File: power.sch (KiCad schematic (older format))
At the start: 25 parts

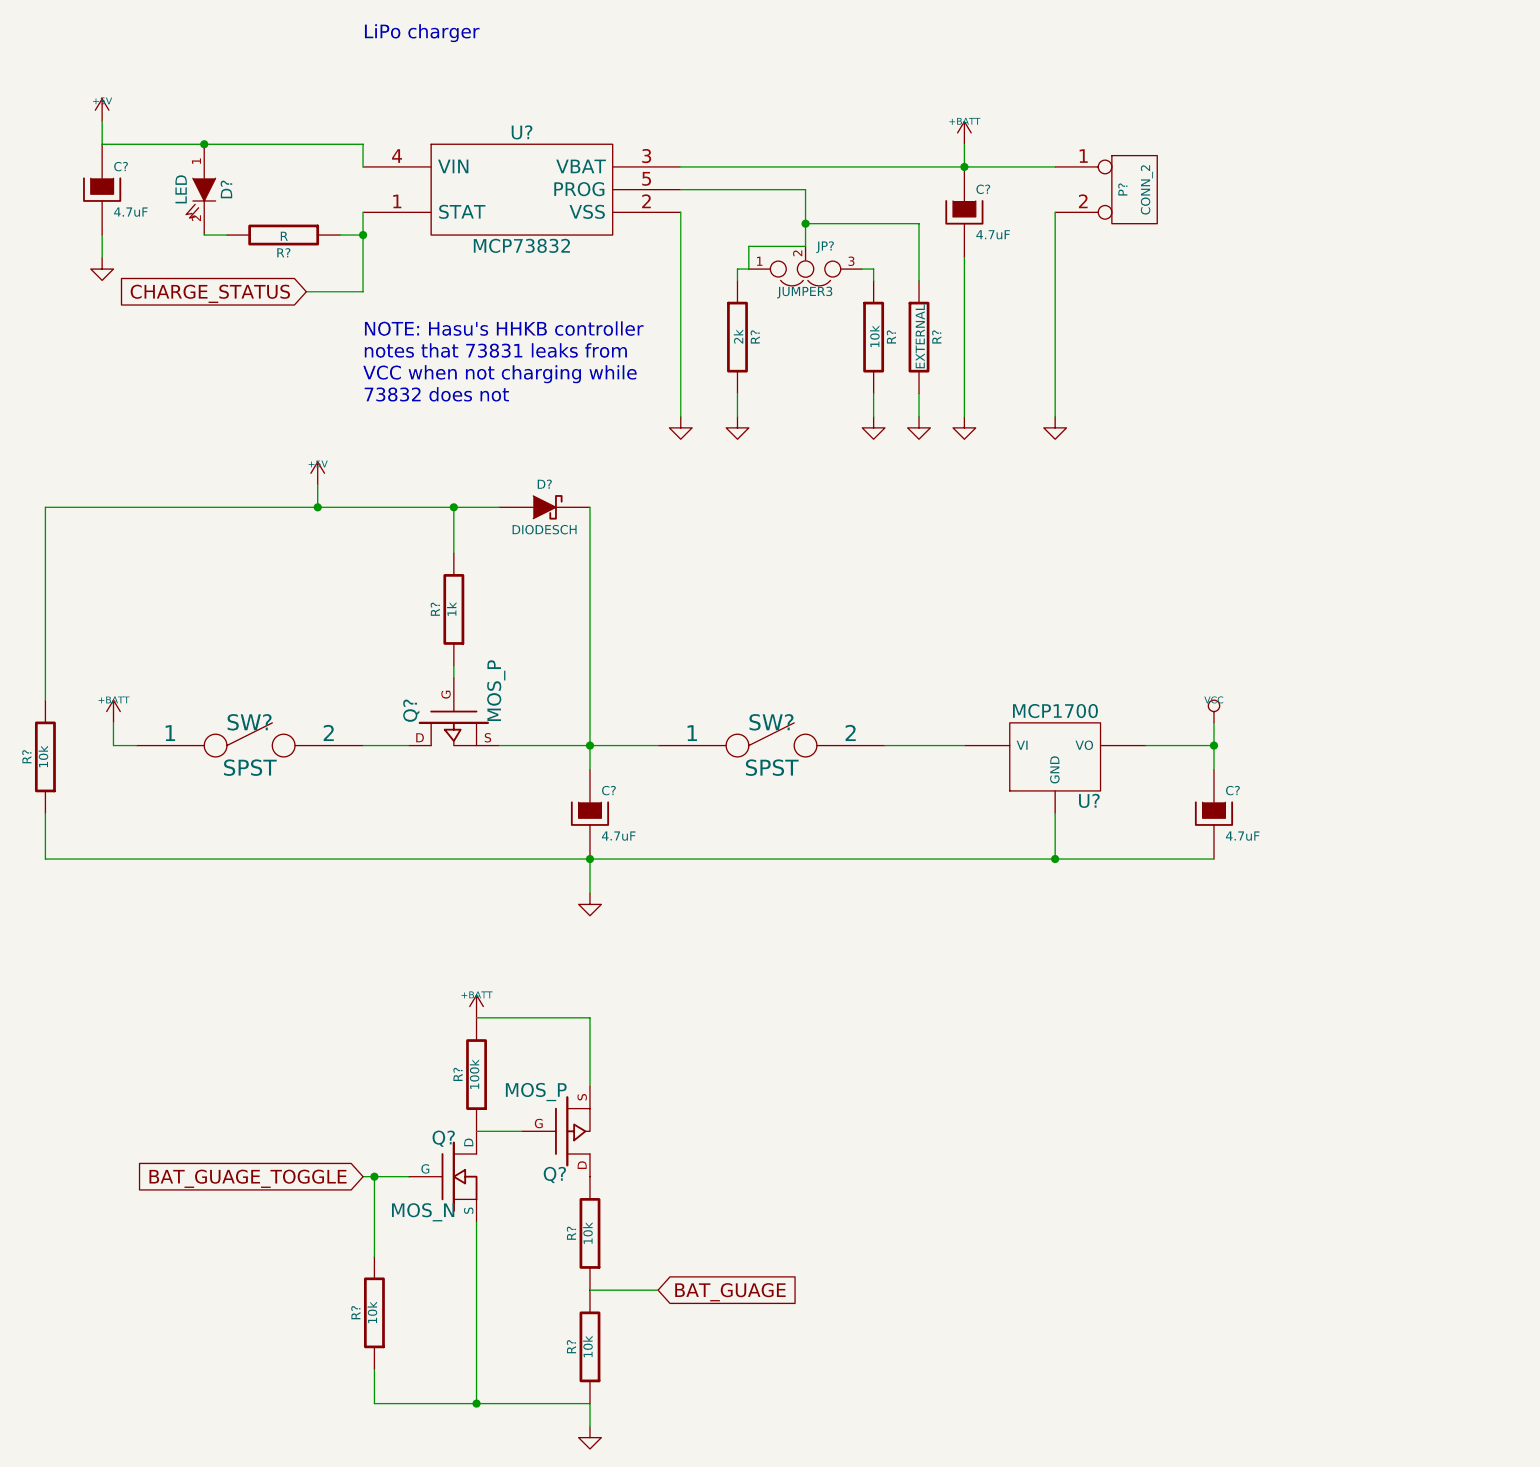
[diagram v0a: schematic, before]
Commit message: Add annotations to parts
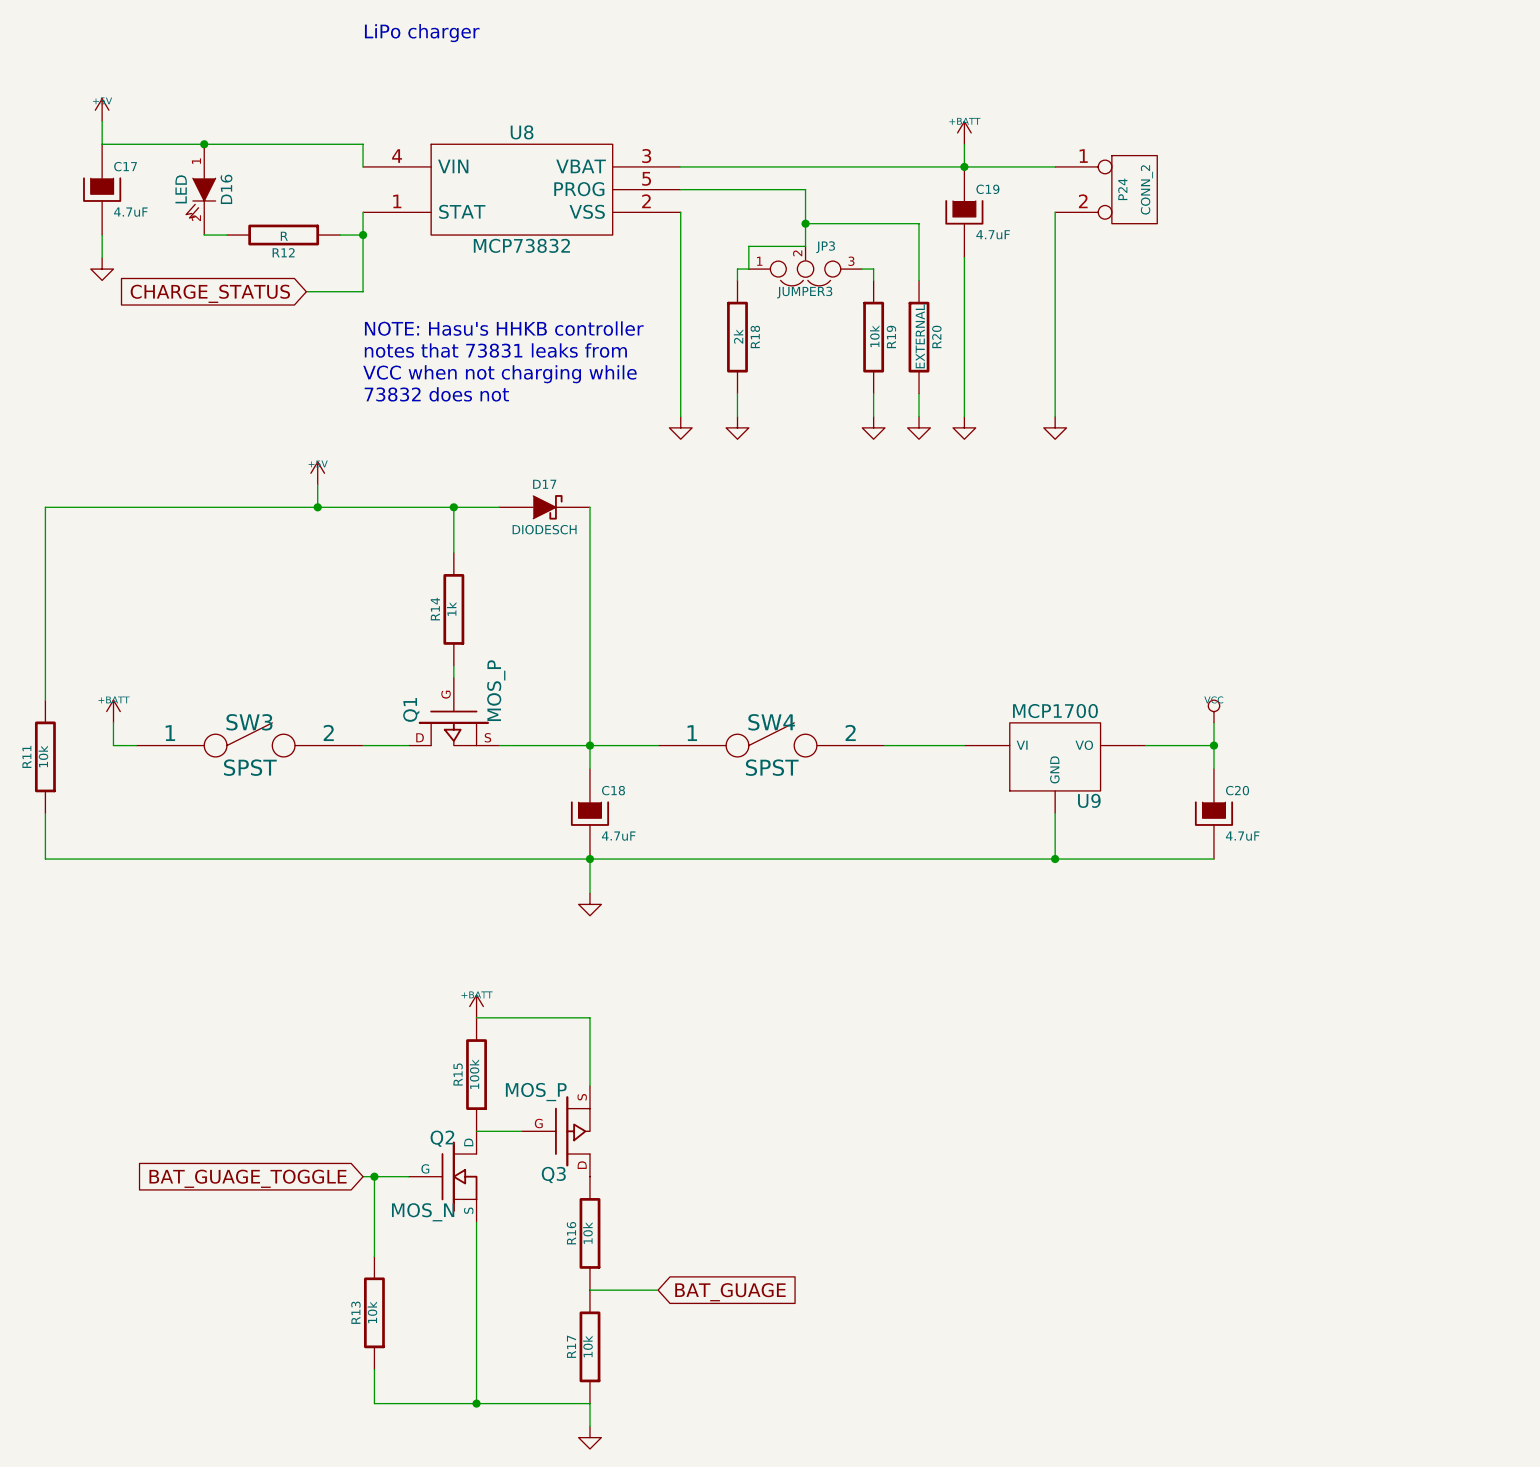
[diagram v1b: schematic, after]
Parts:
- gave numbers to parts that had none: 25
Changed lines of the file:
@@
 $EndDescr
 $Comp
-L +5V #PWR?
+L +5V #PWR56
 U 1 1 54E62CDB
 P 1050 1250
-F 0 "#PWR?" H 1050 1340 20  0001 C CNN
+F 0 "#PWR56" H 1050 1340 20  0001 C CNN
 F 1 "+5V" H 1050 1340 30  0000 C CNN
 F 2 "" H 1050 1250 60  0000 C CNN
@@
 $EndComp
 $Comp
-L GND #PWR?
+L GND #PWR57
 U 1 1 54E62CE1
 P 1050 1850
-F 0 "#PWR?" H 1050 1850 30  0001 C CNN
+F 0 "#PWR57" H 1050 1850 30  0001 C CNN
 F 1 "GND" H 1050 1780 30  0001 C CNN
 F 2 "" H 1050 1850 60  0000 C CNN
@@
 $EndComp
 $Comp
-L CP C?
+L CP C17
 U 1 1 54E62CE7
 P 1050 1550
-F 0 "C?" H 1100 1650 40  0000 L CNN
+F 0 "C17" H 1100 1650 40  0000 L CNN
 F 1 "4.7uF" H 1100 1450 40  0000 L CNN
 F 2 "" H 1150 1400 30  0000 C CNN
@@
 $EndComp
 $Comp
-L LED D?
+L LED D16
 U 1 1 54E62CEE
 P 1500 1550
-F 0 "D?" H 1500 1650 50  0000 C CNN
+F 0 "D16" H 1500 1650 50  0000 C CNN
 F 1 "LED" H 1500 1450 50  0000 C CNN
 F 2 "" H 1500 1550 60  0000 C CNN
@@
 $EndComp
 $Comp
-L MCP73831 U?
+L MCP73831 U8
 U 1 1 54E62CF5
 P 2900 1500
-F 0 "U?" H 2900 1700 60  0000 C CNN
+F 0 "U8" H 2900 1700 60  0000 C CNN
 F 1 "MCP73832" H 2900 1200 60  0000 C CNN
 F 2 "" H 2900 1500 60  0000 C CNN
@@
 $EndComp
 $Comp
-L JUMPER3 JP?
+L JUMPER3 JP3
 U 1 1 54E62CFC
 P 4150 1900
-F 0 "JP?" H 4200 1800 40  0000 L CNN
+F 0 "JP3" H 4200 1800 40  0000 L CNN
 F 1 "JUMPER3" H 4150 2000 40  0000 C CNN
 F 2 "" H 4150 1900 60  0000 C CNN
@@
 $EndComp
 $Comp
-L R R?
+L R R18
 U 1 1 54E62D03
 P 3850 2200
-F 0 "R?" V 3930 2200 40  0000 C CNN
+F 0 "R18" V 3930 2200 40  0000 C CNN
 F 1 "2k" V 3857 2201 40  0000 C CNN
 F 2 "" V 3780 2200 30  0000 C CNN
@@
 $EndComp
 $Comp
-L R R?
+L R R19
 U 1 1 54E62D0A
 P 4450 2200
-F 0 "R?" V 4530 2200 40  0000 C CNN
+F 0 "R19" V 4530 2200 40  0000 C CNN
 F 1 "10k" V 4457 2201 40  0000 C CNN
 F 2 "" V 4380 2200 30  0000 C CNN
@@
 $EndComp
 $Comp
-L R R?
+L R R20
 U 1 1 54E62D11
 P 4650 2200
-F 0 "R?" V 4730 2200 40  0000 C CNN
+F 0 "R20" V 4730 2200 40  0000 C CNN
 F 1 "EXTERNAL" V 4657 2201 40  0000 C CNN
 F 2 "" V 4580 2200 30  0000 C CNN
@@
 $EndComp
 $Comp
-L CP C?
+L CP C19
 U 1 1 54E62D18
 P 4850 1650
-F 0 "C?" H 4900 1750 40  0000 L CNN
+F 0 "C19" H 4900 1750 40  0000 L CNN
 F 1 "4.7uF" H 4900 1550 40  0000 L CNN
 F 2 "" H 4950 1500 30  0000 C CNN
@@
 $EndComp
 $Comp
-L R R?
+L R R12
 U 1 1 54E62D1F
 P 1850 1750
-F 0 "R?" V 1930 1750 40  0000 C CNN
+F 0 "R12" V 1930 1750 40  0000 C CNN
 F 1 "R" V 1857 1751 40  0000 C CNN
 F 2 "" V 1780 1750 30  0000 C CNN
@@
 $EndComp
 $Comp
-L GND #PWR?
+L GND #PWR63
 U 1 1 54E62D26
 P 3600 2550
-F 0 "#PWR?" H 3600 2550 30  0001 C CNN
+F 0 "#PWR63" H 3600 2550 30  0001 C CNN
 F 1 "GND" H 3600 2480 30  0001 C CNN
 F 2 "" H 3600 2550 60  0000 C CNN
@@
 $EndComp
 $Comp
-L GND #PWR?
+L GND #PWR64
 U 1 1 54E62D2C
 P 3850 2550
-F 0 "#PWR?" H 3850 2550 30  0001 C CNN
+F 0 "#PWR64" H 3850 2550 30  0001 C CNN
 F 1 "GND" H 3850 2480 30  0001 C CNN
 F 2 "" H 3850 2550 60  0000 C CNN
@@
 $EndComp
 $Comp
-L GND #PWR?
+L GND #PWR65
 U 1 1 54E62D32
 P 4450 2550
-F 0 "#PWR?" H 4450 2550 30  0001 C CNN
+F 0 "#PWR65" H 4450 2550 30  0001 C CNN
 F 1 "GND" H 4450 2480 30  0001 C CNN
 F 2 "" H 4450 2550 60  0000 C CNN
@@
 $EndComp
 $Comp
-L GND #PWR?
+L GND #PWR66
 U 1 1 54E62D38
 P 4650 2550
-F 0 "#PWR?" H 4650 2550 30  0001 C CNN
+F 0 "#PWR66" H 4650 2550 30  0001 C CNN
 F 1 "GND" H 4650 2480 30  0001 C CNN
 F 2 "" H 4650 2550 60  0000 C CNN
@@
 $EndComp
 $Comp
-L GND #PWR?
+L GND #PWR68
 U 1 1 54E62D3E
 P 4850 2550
-F 0 "#PWR?" H 4850 2550 30  0001 C CNN
+F 0 "#PWR68" H 4850 2550 30  0001 C CNN
 F 1 "GND" H 4850 2480 30  0001 C CNN
 F 2 "" H 4850 2550 60  0000 C CNN
@@
 $EndComp
 $Comp
-L +BATT #PWR?
+L +BATT #PWR67
 U 1 1 54E62D44
 P 4850 1350
-F 0 "#PWR?" H 4850 1300 20  0001 C CNN
+F 0 "#PWR67" H 4850 1300 20  0001 C CNN
 F 1 "+BATT" H 4850 1450 30  0000 C CNN
 F 2 "" H 4850 1350 60  0000 C CNN
@@
 $EndComp
 $Comp
-L CONN_2 P?
+L CONN_2 P24
 U 1 1 54E62D4A
 P 5600 1550
-F 0 "P?" V 5550 1550 40  0000 C CNN
+F 0 "P24" V 5550 1550 40  0000 C CNN
 F 1 "CONN_2" V 5650 1550 40  0000 C CNN
 F 2 "" H 5600 1550 60  0000 C CNN
@@
 $EndComp
 $Comp
-L GND #PWR?
+L GND #PWR69
 U 1 1 54E62D51
 P 5250 2550
-F 0 "#PWR?" H 5250 2550 30  0001 C CNN
+F 0 "#PWR69" H 5250 2550 30  0001 C CNN
 F 1 "GND" H 5250 2480 30  0001 C CNN
 F 2 "" H 5250 2550 60  0000 C CNN
@@
 NOTE: Hasu's HHKB controller\nnotes that 73831 leaks from\nVCC when not charging while\n73832 does not
 $Comp
-L MOS_P Q?
+L MOS_P Q3
 U 1 1 54E64257
 P 3100 5700
-F 0 "Q?" H 3100 5890 60  0000 R CNN
+F 0 "Q3" H 3100 5890 60  0000 R CNN
 F 1 "MOS_P" H 3100 5520 60  0000 R CNN
 F 2 "" H 3100 5700 60  0000 C CNN
@@
 $EndComp
 $Comp
-L MOS_N Q?
+L MOS_N Q2
 U 1 1 54E6425E
 P 2600 5900
-F 0 "Q?" H 2610 6070 60  0000 R CNN
+F 0 "Q2" H 2610 6070 60  0000 R CNN
 F 1 "MOS_N" H 2610 5750 60  0000 R CNN
 F 2 "" H 2600 5900 60  0000 C CNN
@@
 $EndComp
 $Comp
-L R R?
+L R R15
 U 1 1 54E64265
 P 2700 5450
-F 0 "R?" V 2780 5450 40  0000 C CNN
+F 0 "R15" V 2780 5450 40  0000 C CNN
 F 1 "100k" V 2707 5451 40  0000 C CNN
 F 2 "" V 2630 5450 30  0000 C CNN
@@
 $EndComp
 $Comp
-L R R?
+L R R16
 U 1 1 54E6426C
 P 3200 6150
-F 0 "R?" V 3280 6150 40  0000 C CNN
+F 0 "R16" V 3280 6150 40  0000 C CNN
 F 1 "10k" V 3207 6151 40  0000 C CNN
 F 2 "" V 3130 6150 30  0000 C CNN
@@
 $EndComp
 $Comp
-L R R?
+L R R17
 U 1 1 54E64273
 P 3200 6650
-F 0 "R?" V 3280 6650 40  0000 C CNN
+F 0 "R17" V 3280 6650 40  0000 C CNN
 F 1 "10k" V 3207 6651 40  0000 C CNN
 F 2 "" V 3130 6650 30  0000 C CNN
@@
 	3200 6400 3500 6400
 $Comp
-L +BATT #PWR?
+L +BATT #PWR60
 U 1 1 54E64283
 P 2700 5200
-F 0 "#PWR?" H 2700 5150 20  0001 C CNN
+F 0 "#PWR60" H 2700 5150 20  0001 C CNN
 F 1 "+BATT" H 2700 5300 30  0000 C CNN
 F 2 "" H 2700 5200 60  0000 C CNN
@@
 $EndComp
 $Comp
-L GND #PWR?
+L GND #PWR62
 U 1 1 54E64289
 P 3200 7000
-F 0 "#PWR?" H 3200 7000 30  0001 C CNN
+F 0 "#PWR62" H 3200 7000 30  0001 C CNN
 F 1 "GND" H 3200 6930 30  0001 C CNN
 F 2 "" H 3200 7000 60  0000 C CNN
@@
 	3200 6900 3200 7000
 $Comp
-L MOS_P Q?
+L MOS_P Q1
 U 1 1 54E64290
 P 2600 3900
-F 0 "Q?" H 2600 4090 60  0000 R CNN
+F 0 "Q1" H 2600 4090 60  0000 R CNN
 F 1 "MOS_P" H 2600 3720 60  0000 R CNN
 F 2 "" H 2600 3900 60  0000 C CNN
@@
 $EndComp
 $Comp
-L +BATT #PWR?
+L +BATT #PWR58
 U 1 1 54E64297
 P 1100 3900
-F 0 "#PWR?" H 1100 3850 20  0001 C CNN
+F 0 "#PWR58" H 1100 3850 20  0001 C CNN
 F 1 "+BATT" H 1100 4000 30  0000 C CNN
 F 2 "" H 1100 3900 60  0000 C CNN
@@
 $EndComp
 $Comp
-L CP C?
+L CP C18
 U 1 1 54E6429D
 P 3200 4300
-F 0 "C?" H 3250 4400 40  0000 L CNN
+F 0 "C18" H 3250 4400 40  0000 L CNN
 F 1 "4.7uF" H 3250 4200 40  0000 L CNN
 F 2 "" H 3300 4150 30  0000 C CNN
@@
 $EndComp
 $Comp
-L DIODESCH D?
+L DIODESCH D17
 U 1 1 54E642A4
 P 3000 2950
-F 0 "D?" H 3000 3050 40  0000 C CNN
+F 0 "D17" H 3000 3050 40  0000 C CNN
 F 1 "DIODESCH" H 3000 2850 40  0000 C CNN
 F 2 "" H 3000 2950 60  0000 C CNN
@@
 $EndComp
 $Comp
-L MCP1700 U?
+L MCP1700 U9
 U 1 1 54E642AB
 P 5250 4050
-F 0 "U?" H 5400 3854 60  0000 C CNN
+F 0 "U9" H 5400 3854 60  0000 C CNN
 F 1 "MCP1700" H 5250 4250 60  0000 C CNN
 F 2 "" H 5250 4050 60  0000 C CNN
@@
 $EndComp
 $Comp
-L VCC #PWR?
+L VCC #PWR70
 U 1 1 54E642B2
 P 5950 3900
-F 0 "#PWR?" H 5950 4000 30  0001 C CNN
+F 0 "#PWR70" H 5950 4000 30  0001 C CNN
 F 1 "VCC" H 5950 4000 30  0000 C CNN
 F 2 "" H 5950 3900 60  0000 C CNN
@@
 	800  2950 2800 2950
 $Comp
-L +5V #PWR?
+L +5V #PWR59
 U 1 1 54E642BF
 P 2000 2850
-F 0 "#PWR?" H 2000 2940 20  0001 C CNN
+F 0 "#PWR59" H 2000 2940 20  0001 C CNN
 F 1 "+5V" H 2000 2940 30  0000 C CNN
 F 2 "" H 2000 2850 60  0000 C CNN
@@
 	5950 3900 5950 4100
 $Comp
-L GND #PWR?
+L GND #PWR61
 U 1 1 54E642C9
 P 3200 4650
-F 0 "#PWR?" H 3200 4650 30  0001 C CNN
+F 0 "#PWR61" H 3200 4650 30  0001 C CNN
 F 1 "GND" H 3200 4580 30  0001 C CNN
 F 2 "" H 3200 4650 60  0000 C CNN
@@
 	800  4500 5950 4500
 $Comp
-L R R?
+L R R11
 U 1 1 54E642D2
 P 800 4050
-F 0 "R?" V 880 4050 40  0000 C CNN
+F 0 "R11" V 880 4050 40  0000 C CNN
 F 1 "10k" V 807 4051 40  0000 C CNN
 F 2 "" V 730 4050 30  0000 C CNN
@@
 Connection ~ 3200 4500
 $Comp
-L CP C?
+L CP C20
 U 1 1 54E642DD
 P 5950 4300
-F 0 "C?" H 6000 4400 40  0000 L CNN
+F 0 "C20" H 6000 4400 40  0000 L CNN
 F 1 "4.7uF" H 6000 4200 40  0000 L CNN
 F 2 "" H 6050 4150 30  0000 C CNN
@@
 Connection ~ 5950 4000
 $Comp
-L SPST SW?
+L SPST SW3
 U 1 1 54E81B6B
 P 1700 4000
-F 0 "SW?" H 1700 4100 70  0000 C CNN
+F 0 "SW3" H 1700 4100 70  0000 C CNN
 F 1 "SPST" H 1700 3900 70  0000 C CNN
 F 2 "" H 1700 4000 60  0000 C CNN
@@
 Connection ~ 2200 1750
 $Comp
-L R R?
+L R R14
 U 1 1 54E977E3
 P 2600 3400
-F 0 "R?" V 2680 3400 40  0000 C CNN
+F 0 "R14" V 2680 3400 40  0000 C CNN
 F 1 "1k" V 2607 3401 40  0000 C CNN
 F 2 "" V 2530 3400 30  0000 C CNN
@@
 	2600 3650 2600 3700
 $Comp
-L R R?
+L R R13
 U 1 1 54E98880
 P 2250 6500
-F 0 "R?" V 2330 6500 40  0000 C CNN
+F 0 "R13" V 2330 6500 40  0000 C CNN
 F 1 "10k" V 2257 6501 40  0000 C CNN
 F 2 "" V 2180 6500 30  0000 C CNN
@@
 Connection ~ 2700 6900
 $Comp
-L SPST SW?
+L SPST SW4
 U 1 1 54E9976A
 P 4000 4000
-F 0 "SW?" H 4000 4100 70  0000 C CNN
+F 0 "SW4" H 4000 4100 70  0000 C CNN
 F 1 "SPST" H 4000 3900 70  0000 C CNN
 F 2 "" H 4000 4000 60  0000 C CNN
